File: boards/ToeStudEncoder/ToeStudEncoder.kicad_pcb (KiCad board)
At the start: 2 copper layers, 95 x 58 mm, 28 parts, among them J1 Swell, J2 ISP, J3 ToeLeft, J4 ToeRight, J5 MIDI In, J8 MIDI Out, J9 Controller, Q1 BC547, U1 ATmega48-20P, U2 6N137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

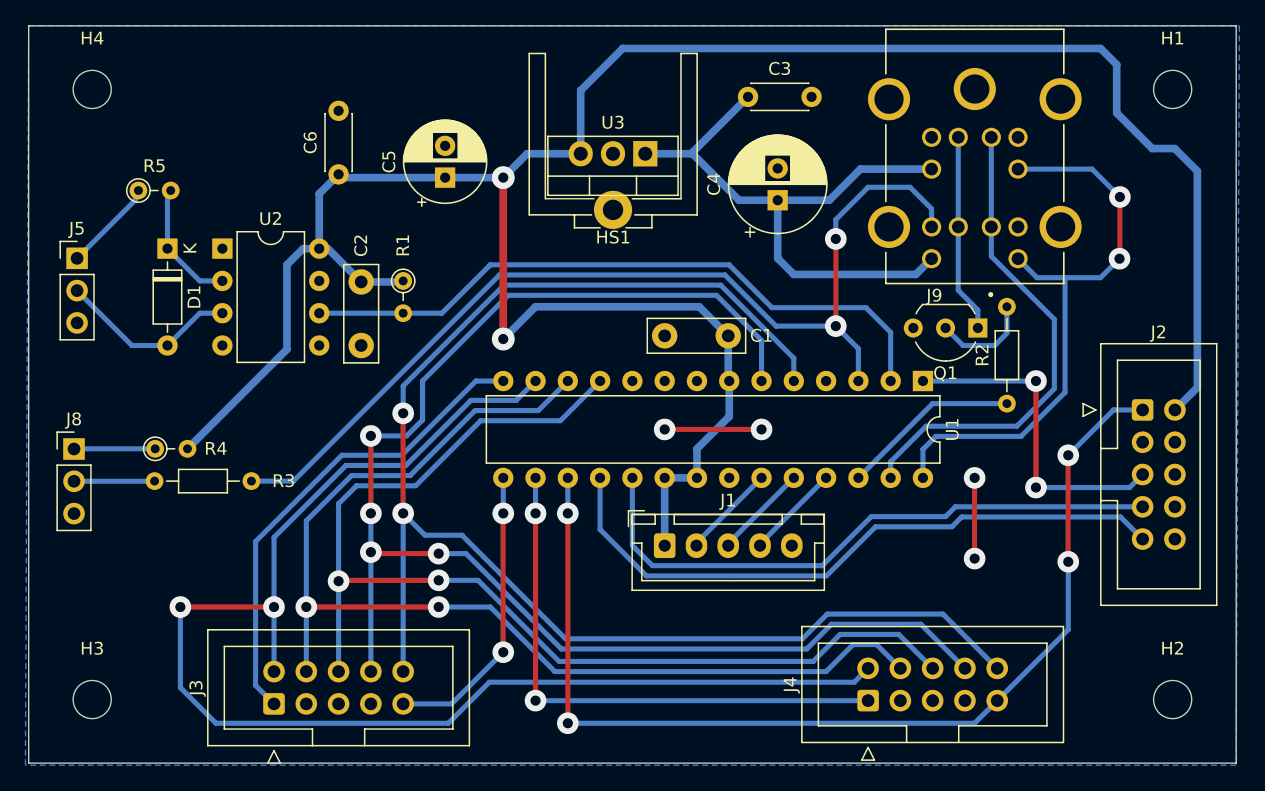
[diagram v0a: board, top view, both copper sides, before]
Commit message: Updated design rules to 0.32mm template and exported Gerber files
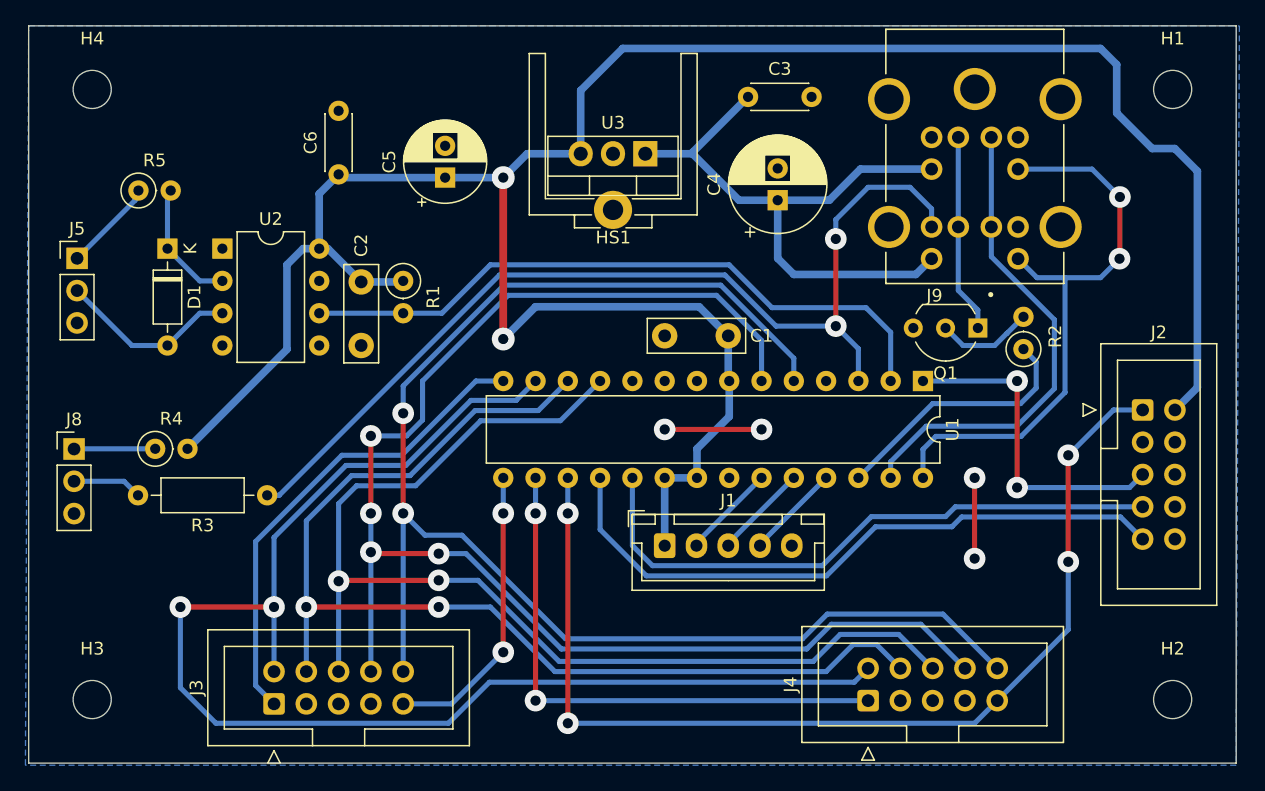
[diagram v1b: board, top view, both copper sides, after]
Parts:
- R1, R4, R5: footprint Resistor_THT:R_Axial_DIN0204_L3.6mm_D1.6mm_P2.54mm_Vertical -> Resistor_THT:R_Axial_DIN0207_L6.3mm_D2.5mm_P2.54mm_Vertical
- R2: footprint Resistor_THT:R_Axial_DIN0204_L3.6mm_D1.6mm_P7.62mm_Horizontal -> Resistor_THT:R_Axial_DIN0207_L6.3mm_D2.5mm_P2.54mm_Vertical
- R3: footprint Resistor_THT:R_Axial_DIN0204_L3.6mm_D1.6mm_P7.62mm_Horizontal -> Resistor_THT:R_Axial_DIN0207_L6.3mm_D2.5mm_P10.16mm_Horizontal
- moved R2 4.48 mm to (188.5, 77.5)
- moved R3 1.67 mm to (129.0, 89.0)
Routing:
- net Interrupt: track 14.1 -> 20.4 mm
- net Net-(J8-Pin_2): track 6.32 -> 5.49 mm
- net TXD: track 78.5 -> 77.7 mm

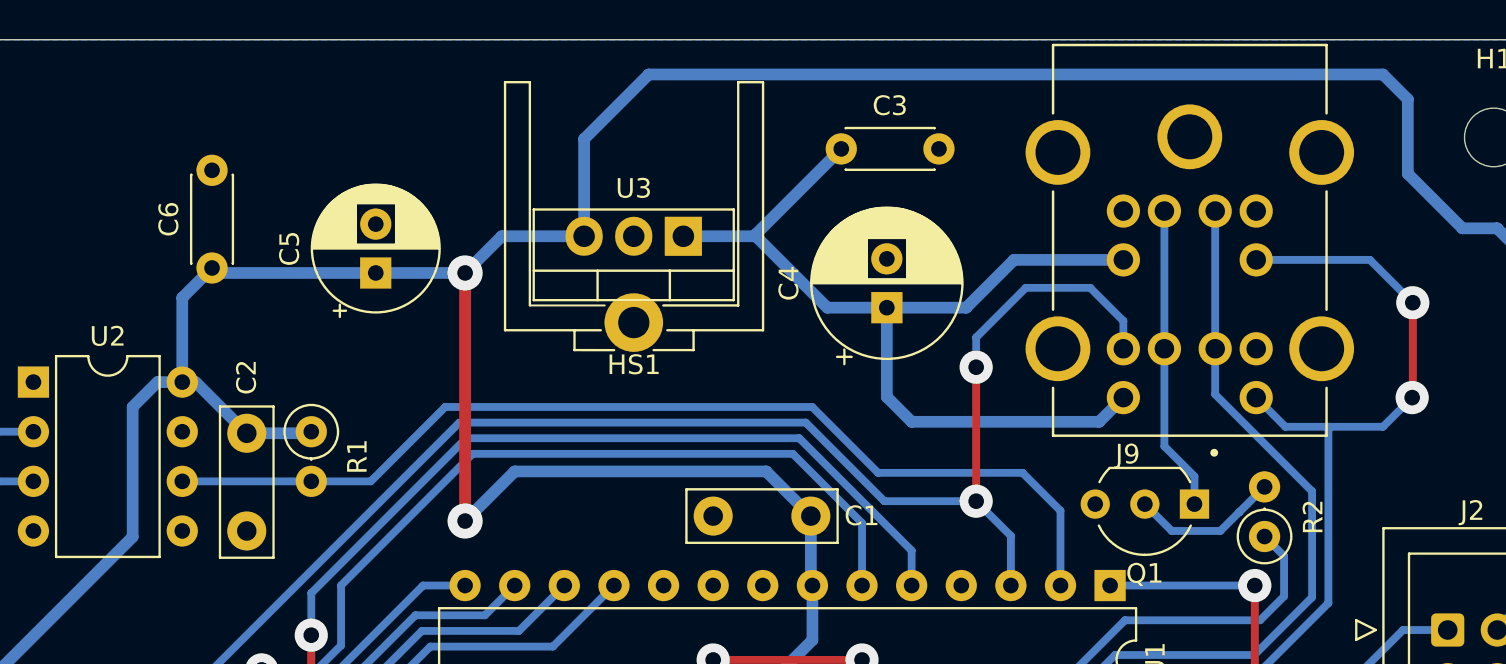
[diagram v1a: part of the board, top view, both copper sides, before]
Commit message: Make Toestud PS2 connectors symmetrical to avoid connection errors
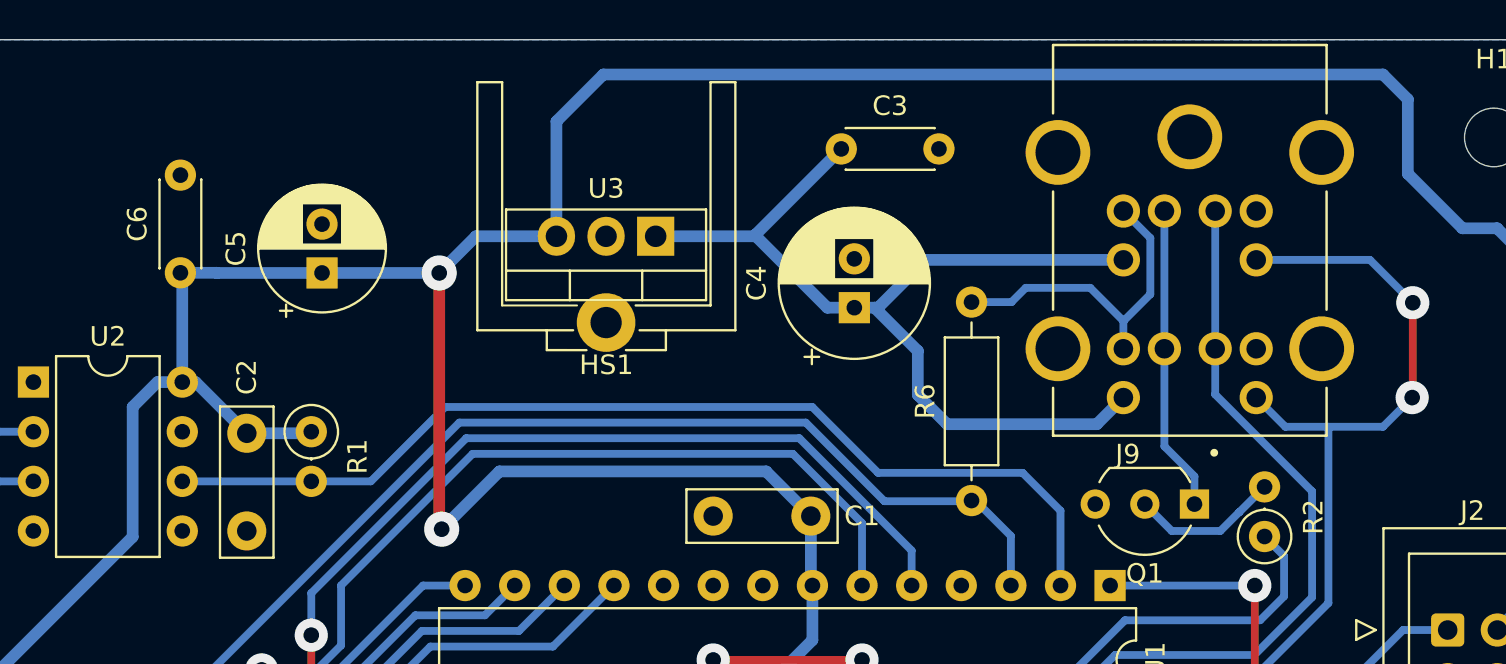
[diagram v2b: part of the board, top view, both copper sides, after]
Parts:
- added R6: 220, Resistor_THT:R_Axial_DIN0207_L6.3mm_D2.5mm_P10.16mm_Horizontal, F.Cu at (173.5, 75.7)
- moved C5 2.75 mm to (140.2, 64.0)
- moved C4 1.66 mm to (167.5, 65.8)
- moved C6 1.64 mm to (133.0, 64.0)
- moved HS1 1.42 mm to (154.8, 65.7)
- moved U3 1.42 mm to (157.3, 62.1)
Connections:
- J9 pad 4_1: unconnected-(J9-Pad4_1) -> Net-(J9-Pad4_1)
- J9 pad 4_2: TXD -> Net-(J9-Pad4_1)
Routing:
- net TXD: track 77.7 -> 58.6 mm, vias 2 -> 0
- net Net-(J9-Pad4_1): track 0.00 -> 17.0 mm
- net +5V: track 187.7 -> 191.0 mm
- net +12V: track 49.1 -> 49.8 mm

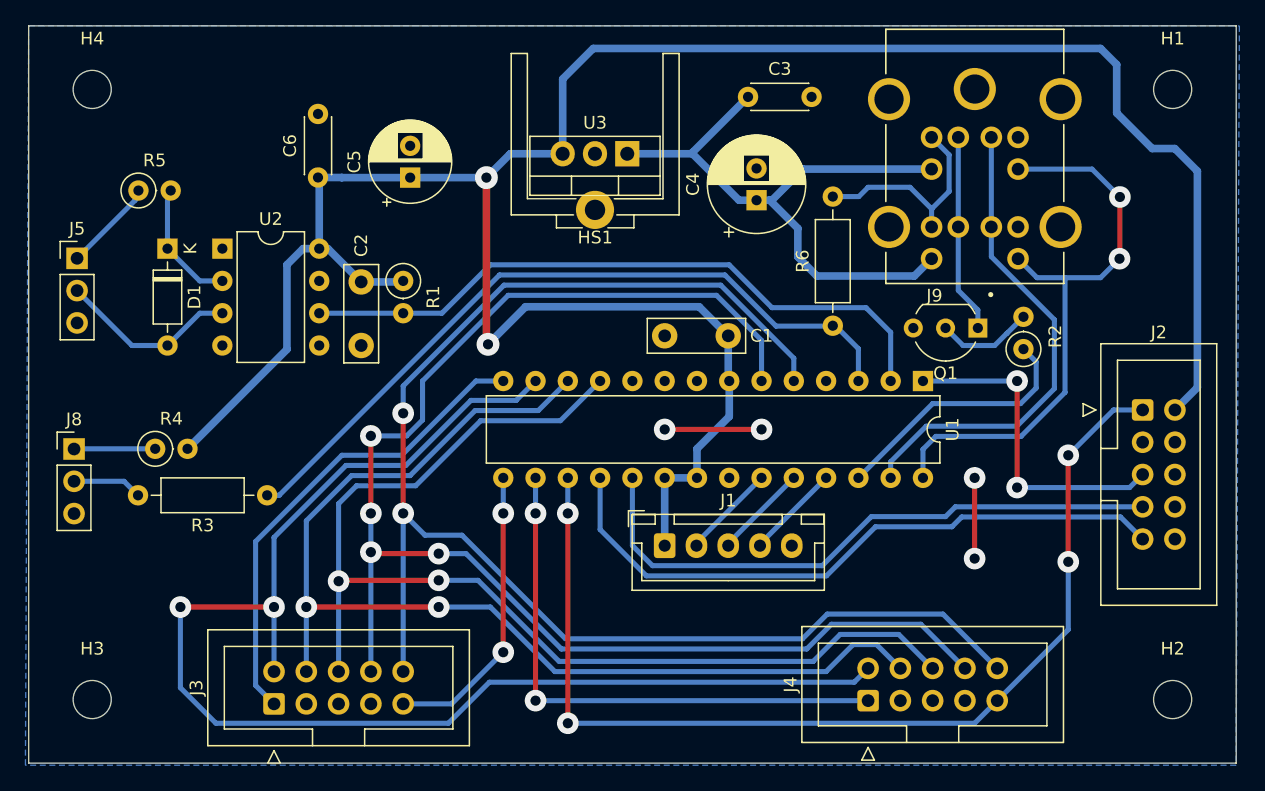
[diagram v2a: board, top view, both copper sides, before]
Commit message: ToeStudEncoder: Fixed mirrored PS2 pinout
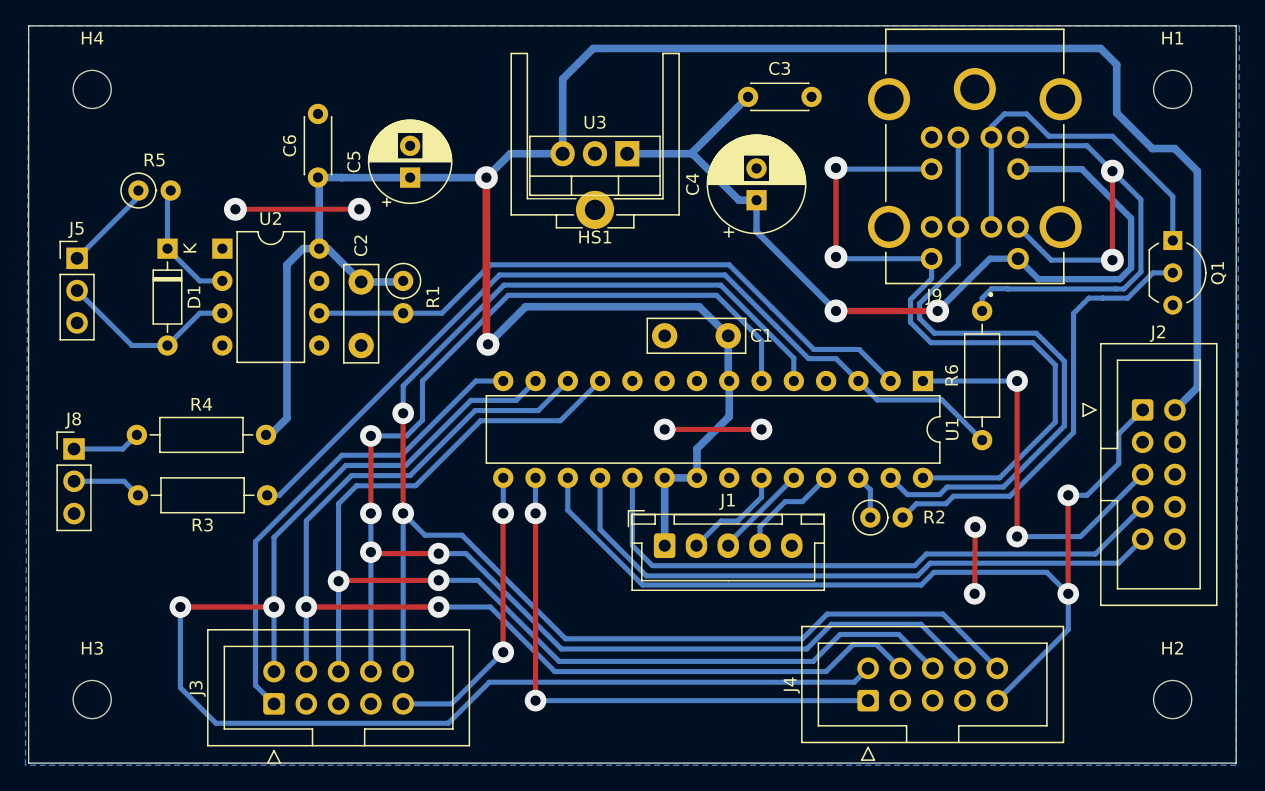
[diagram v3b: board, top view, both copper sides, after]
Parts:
- R4: footprint Resistor_THT:R_Axial_DIN0207_L6.3mm_D2.5mm_P2.54mm_Vertical -> Resistor_THT:R_Axial_DIN0207_L6.3mm_D2.5mm_P10.16mm_Horizontal
- moved R2 17.9 mm to (176.5, 90.8), turned to 0 degrees
- moved Q1 16.8 mm to (200.2, 69.0), turned to -90 degrees
- moved R6 14.8 mm to (185.2, 84.7)
- moved R4 1.81 mm to (118.8, 84.2)
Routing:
- net Net-(J9-Pad4_1): track 17.0 -> 47.5 mm, vias 0 -> 2
- net Net-(Q1-B): track 7.63 -> 34.4 mm
- net +12V: track 49.8 -> 69.6 mm, vias 0 -> 2
- net Interrupt: track 20.4 -> 3.51 mm
- net Net-(Q1-C): track 15.6 -> 28.7 mm
- net SDA: track 38.4 -> 49.8 mm
- net TXD: track 58.6 -> 68.8 mm
- net SCL: track 47.3 -> 57.3 mm
- net MOSI: track 82.8 -> 73.9 mm, vias 4 -> 2
- net GND: track 14.0 -> 22.6 mm, vias 4 -> 6
- net Reset: track 26.1 -> 31.5 mm
- net +5V: track 191.0 -> 187.6 mm
- net RXD: track 52.6 -> 50.9 mm
- net MISO: track 50.9 -> 49.5 mm
- net Net-(J1-Pin_2): track 7.24 -> 8.22 mm
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
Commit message: Disconnected UART lines to avoid interference
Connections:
- J9 pad 4_2: Net-(J9-Pad4_1) -> unconnected-(J9-Pad4_2)
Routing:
- net Net-(J9-Pad4_1): track 47.5 -> 32.0 mm, vias 2 -> 0
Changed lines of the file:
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@@
 	(net 43 "unconnected-(U2-NC-Pad4)")
 	(net 44 "unconnected-(U2-EN-Pad7)")
-	(net 45 "Net-(J9-Pad4_1)")
-	(net 46 "Net-(Q1-B)")
+	(net 45 "Net-(Q1-B)")
+	(net 46 "Net-(J9-Pad4_1)")
+	(net 47 "unconnected-(J9-Pad4_2)")
 	(footprint "SnapEDA:SWITCHCRAFT_DMD6FRA111"
 		(layer "F.Cu")
@@
 			(layers "*.Cu" "*.Mask")
 			(remove_unused_layers no)
-			(net 45 "Net-(J9-Pad4_1)")
+			(net 46 "Net-(J9-Pad4_1)")
 			(pintype "passive")
 			(solder_mask_margin 0.102)
@@
 			(layers "*.Cu" "*.Mask")
 			(remove_unused_layers no)
-			(net 45 "Net-(J9-Pad4_1)")
-			(pintype "passive")
+			(net 47 "unconnected-(J9-Pad4_2)")
+			(pintype "passive+no_connect")
 			(solder_mask_margin 0.102)
 		)
@@
 		(tags "Resistor Axial_DIN0207 series Axial Vertical pin pitch 2.54mm 0.25W = 1/4W length 6.3mm diameter 2.5mm")
 		(property "Reference" "R2"
-			(at 5.04 0 360)
+			(at 5.04 0 0)
 			(layer "F.SilkS")
 			(effects
@@
 		)
 		(property "Value" "4k7"
-			(at -2.96 0.25 360)
+			(at -2.96 0.25 0)
 			(layer "F.Fab")
 			(effects
@@
 		)
 		(fp_text user "${REFERENCE}"
-			(at 5.04 0 360)
+			(at 5.04 0 0)
 			(layer "F.Fab")
 			(effects
@@
 			(layers "*.Cu" "*.Mask")
 			(remove_unused_layers no)
-			(net 46 "Net-(Q1-B)")
+			(net 45 "Net-(Q1-B)")
 			(pintype "passive")
 		)
@@
 			(layers "*.Cu" "*.Mask")
 			(remove_unused_layers no)
-			(net 46 "Net-(Q1-B)")
+			(net 45 "Net-(Q1-B)")
 			(pinfunction "B")
 			(pintype "input")
@@
 			(layers "*.Cu" "*.Mask")
 			(remove_unused_layers no)
-			(net 45 "Net-(J9-Pad4_1)")
+			(net 46 "Net-(J9-Pad4_1)")
 			(pintype "passive")
 		)
@@
 	)
 	(segment
-		(start 195.5 70.5)
-		(end 195.5 63.5)
-		(width 0.4)
-		(layer "F.Cu")
-		(net 45)
-	)
-	(via
-		(at 195.5 70.5)
-		(size 1.8)
-		(drill 0.8)
-		(layers "F.Cu" "B.Cu")
-		(net 45)
-	)
-	(via
-		(at 195.5 63.5)
-		(size 1.8)
-		(drill 0.8)
-		(layers "F.Cu" "B.Cu")
-		(net 45)
-	)
-	(segment
-		(start 188.073 60.839)
-		(end 188.734 61.5)
-		(width 0.4)
-		(layer "B.Cu")
-		(net 45)
-	)
-	(segment
-		(start 195.759949 72.769999)
-		(end 187.269999 72.769999)
-		(width 0.4)
-		(layer "B.Cu")
-		(net 45)
-	)
-	(segment
-		(start 188.734 61.5)
-		(end 193.5 61.5)
+		(start 192.44 74.69)
+		(end 193.640001 73.489999)
 		(width 0.4)
 		(layer "B.Cu")
@@
 	)
 	(segment
-		(start 195.5 63.5)
-		(end 197.739999 65.739999)
+		(start 183 89.07)
+		(end 187.43 89.07)
 		(width 0.4)
 		(layer "B.Cu")
@@
 	)
 	(segment
-		(start 193.5 61.5)
-		(end 195.5 63.5)
+		(start 194.75 73.489999)
+		(end 194.750001 73.49)
 		(width 0.4)
 		(layer "B.Cu")
@@
 	)
 	(segment
-		(start 196.397838 72.77)
-		(end 195.759949 72.769999)
+		(start 182.4 89.67)
+		(end 183 89.07)
 		(width 0.4)
 		(layer "B.Cu")
@@
 	)
 	(segment
-		(start 187.269999 72.769999)
-		(end 187.25 72.75)
+		(start 193.640001 73.489999)
+		(end 194.75 73.489999)
 		(width 0.4)
 		(layer "B.Cu")
@@
 	)
 	(segment
-		(start 186 72.75)
-		(end 185.25 73.5)
+		(start 187.43 89.07)
+		(end 192.44 84.06)
 		(width 0.4)
 		(layer "B.Cu")
@@
 	)
 	(segment
-		(start 187.25 72.75)
-		(end 186 72.75)
+		(start 178.995 90.75)
+		(end 180.075 89.67)
 		(width 0.4)
 		(layer "B.Cu")
@@
 	)
 	(segment
-		(start 188.073 67.889)
-		(end 190.684 70.5)
+		(start 192.44 84.06)
+		(end 192.44 74.69)
 		(width 0.4)
 		(layer "B.Cu")
@@
 	)
 	(segment
-		(start 197.739999 65.739999)
-		(end 197.739999 71.427839)
+		(start 180.075 89.67)
+		(end 182.4 89.67)
 		(width 0.4)
 		(layer "B.Cu")
@@
 	)
 	(segment
-		(start 197.739999 71.427839)
-		(end 196.397838 72.77)
+		(start 196.696072 73.49)
+		(end 198.686072 71.5)
 		(width 0.4)
 		(layer "B.Cu")
@@
 	)
 	(segment
-		(start 190.684 70.5)
-		(end 195.5 70.5)
+		(start 194.750001 73.49)
+		(end 196.696072 73.49)
 		(width 0.4)
 		(layer "B.Cu")
@@
 	)
 	(segment
-		(start 185.25 73.5)
-		(end 185.25 74.75)
+		(start 198.686072 71.5)
+		(end 199.89 71.5)
 		(width 0.4)
 		(layer "B.Cu")
@@
 	)
 	(segment
-		(start 192.44 74.69)
-		(end 193.640001 73.489999)
-		(width 0.4)
-		(layer "B.Cu")
-		(net 46)
-	)
-	(segment
-		(start 183 89.07)
-		(end 187.43 89.07)
+		(start 196.397838 72.77)
+		(end 197.739999 71.427839)
 		(width 0.4)
 		(layer "B.Cu")
@@
 	)
 	(segment
-		(start 194.75 73.489999)
-		(end 194.750001 73.49)
+		(start 197.739999 71.427839)
+		(end 197.739999 65.739999)
 		(width 0.4)
 		(layer "B.Cu")
@@
 	)
 	(segment
-		(start 182.4 89.67)
-		(end 183 89.07)
+		(start 197.739999 65.739999)
+		(end 193.5 61.5)
 		(width 0.4)
 		(layer "B.Cu")
@@
 	)
 	(segment
-		(start 193.640001 73.489999)
-		(end 194.75 73.489999)
+		(start 185.25 73.5)
+		(end 186 72.75)
 		(width 0.4)
 		(layer "B.Cu")
@@
 	)
 	(segment
-		(start 187.43 89.07)
-		(end 192.44 84.06)
+		(start 188.734 61.5)
+		(end 188.073 60.839)
 		(width 0.4)
 		(layer "B.Cu")
@@
 	)
 	(segment
-		(start 178.995 90.75)
-		(end 180.075 89.67)
+		(start 195.759949 72.769999)
+		(end 196.397838 72.77)
 		(width 0.4)
 		(layer "B.Cu")
@@
 	)
 	(segment
-		(start 192.44 84.06)
-		(end 192.44 74.69)
+		(start 186 72.75)
+		(end 187.25 72.75)
 		(width 0.4)
 		(layer "B.Cu")
@@
 	)
 	(segment
-		(start 180.075 89.67)
-		(end 182.4 89.67)
+		(start 185.25 74.75)
+		(end 185.25 73.5)
 		(width 0.4)
 		(layer "B.Cu")
@@
 	)
 	(segment
-		(start 196.696072 73.49)
-		(end 198.686072 71.5)
+		(start 187.25 72.75)
+		(end 187.269999 72.769999)
 		(width 0.4)
 		(layer "B.Cu")
@@
 	)
 	(segment
-		(start 194.750001 73.49)
-		(end 196.696072 73.49)
+		(start 193.5 61.5)
+		(end 188.734 61.5)
 		(width 0.4)
 		(layer "B.Cu")
@@
 	)
 	(segment
-		(start 198.686072 71.5)
-		(end 199.89 71.5)
+		(start 187.269999 72.769999)
+		(end 195.759949 72.769999)
 		(width 0.4)
 		(layer "B.Cu")
